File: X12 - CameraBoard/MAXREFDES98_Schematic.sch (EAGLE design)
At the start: 24 parts, among them U1 MB110S-TP, U2 MB110S-TP, U3 MAX5969AETB+, U4 MAX17503ATP+

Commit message: Added Net Labels & Mounting Holes
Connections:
- net N$1 renamed SV2_1
- net N$10 renamed PG_EN/UVLO
- net N$12 renamed RESET
- net N$13 renamed SS
- net N$14 renamed CF
- net N$16 renamed RT
- net N$17 renamed BST
- net N$18 renamed LX
- net N$19 renamed FB
- net N$2 renamed SV2_2
- net N$21 renamed SV1_1/2
- net N$25 renamed EPAD
- net N$3 renamed SV2_3
- net N$4 renamed SV2_4
- net N$5 renamed VDD
- net N$6 renamed VSS_EP
- net N$7 renamed DET
- net N$8 renamed CLS
- net N$9 renamed VIN

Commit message: rewiring
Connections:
- net N$11 renamed VCC
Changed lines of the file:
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@@
 </segment>
 </net>
-<net name="N$11" class="0">
+<net name="VCC" class="0">
 <segment>
 <pinref part="U4" gate="A" pin="VCC"/>

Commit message: Reconfigured Board Layout
Reconfigured Board Layout
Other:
- note added: "IC PoE CNTRL 1 Channel"
- note added: "IC REG BUCK"
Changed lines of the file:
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@@
 <sheet>
 <plain>
+<text x="137.16" y="7.62" size="1.778" layer="91">IC PoE CNTRL 1 Channel</text>
+<text x="-5.08" y="7.62" size="1.778" layer="91">IC REG BUCK</text>
 </plain>
 <instances>

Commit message: Update MAXREFDES98_Schematic.sch
Added frame and better labels
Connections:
- net SV1_1/2 renamed 5V_OUT
- net SV2_1 renamed RECT_A_INPUT_1
- net SV2_2 renamed RECT_A_INPUT_2
- net SV2_3 renamed RECT_B_INPUT_1
- net SV2_4 renamed RECT_B_INPUT_2
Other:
- note added: "Rectifiers"
- moved on the sheet: SV1
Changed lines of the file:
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@@
 <part name="GND13" library="supply1" library_urn="urn:adsk.eagle:library:371" deviceset="GND" device=""/>
 <part name="L1" library="SD53-3R3-R" deviceset="SD53-3R3-R" device=""/>
+<part name="FRAME1" library="frames" library_urn="urn:adsk.eagle:library:229" deviceset="FRAME_B_L" device=""/>
 </parts>
 <sheets>
 <sheet>
 <plain>
-<text x="137.16" y="7.62" size="1.778" layer="91">IC PoE CNTRL 1 Channel</text>
-<text x="-5.08" y="7.62" size="1.778" layer="91">IC REG BUCK</text>
+<text x="-7.62" y="10.16" size="1.778" layer="91">IC PoE CNTRL 1 Channel</text>
+<text x="142.24" y="7.62" size="1.778" layer="91">IC REG BUCK</text>
+<text x="-109.22" y="-7.62" size="1.778" layer="91">Rectifiers</text>
 </plain>
 <instances>
@@
 <attribute name="VALUE" x="-88.9" y="-5.08" size="1.27" layer="96" rot="R90"/>
 </instance>
-<instance part="SV1" gate="1" x="172.72" y="-86.36" smashed="yes" rot="MR90">
-<attribute name="VALUE" x="160.02" y="-87.63" size="1.778" layer="96" rot="MR90"/>
-<attribute name="NAME" x="181.102" y="-87.63" size="1.778" layer="95" rot="MR90"/>
+<instance part="SV1" gate="1" x="182.88" y="-73.66" smashed="yes" rot="MR90">
+<attribute name="VALUE" x="170.18" y="-74.93" size="1.778" layer="96" rot="MR90"/>
+<attribute name="NAME" x="191.262" y="-74.93" size="1.778" layer="95" rot="MR90"/>
 </instance>
 <instance part="SV2" gate="1" x="-106.68" y="-40.64" smashed="yes" rot="MR90">
@@
 <attribute name="VALUE" x="256.54" y="-48.26" size="1.778" layer="96" rot="MR0"/>
 </instance>
-<instance part="GND9" gate="1" x="170.18" y="-71.12" smashed="yes" rot="MR0">
-<attribute name="VALUE" x="172.72" y="-73.66" size="1.778" layer="96" rot="MR0"/>
+<instance part="GND9" gate="1" x="180.34" y="-58.42" smashed="yes" rot="MR0">
+<attribute name="VALUE" x="182.88" y="-60.96" size="1.778" layer="96" rot="MR0"/>
 </instance>
 <instance part="GND10" gate="1" x="226.06" y="-15.24" smashed="yes" rot="MR0">
@@
 <attribute name="NAME" x="55.88" y="24.13" size="1.778" layer="95" font="vector" rot="R90"/>
 <attribute name="VALUE" x="60.96" y="24.13" size="1.778" layer="96" font="vector" rot="R90" align="top-left"/>
+</instance>
+<instance part="FRAME1" gate="G$1" x="-139.7" y="-144.78" smashed="yes"/>
+<instance part="FRAME1" gate="G$2" x="185.42" y="-144.78" smashed="yes">
+<attribute name="LAST_DATE_TIME" x="198.12" y="-143.51" size="2.54" layer="94"/>
+<attribute name="SHEET" x="271.78" y="-143.51" size="2.54" layer="94"/>
+<attribute name="DRAWING_NAME" x="203.2" y="-125.73" size="2.54" layer="94"/>
 </instance>
 </instances>
@@
 </busses>
 <nets>
-<net name="SV2_1" class="0">
+<net name="RECT_A_INPUT_1" class="0">
 <segment>
 <pinref part="U1" gate="G$1" pin="~1"/>
@@
 </segment>
 </net>
-<net name="SV2_2" class="0">
+<net name="RECT_A_INPUT_2" class="0">
 <segment>
 <pinref part="U1" gate="G$1" pin="~2"/>
@@
 </segment>
 </net>
-<net name="SV2_3" class="0">
+<net name="RECT_B_INPUT_1" class="0">
 <segment>
 <pinref part="U2" gate="G$1" pin="~1"/>
@@
 </segment>
 </net>
-<net name="SV2_4" class="0">
+<net name="RECT_B_INPUT_2" class="0">
 <segment>
 <pinref part="U2" gate="G$1" pin="~2"/>
@@
 <junction x="-25.4" y="22.86"/>
 <pinref part="L1" gate="G$1" pin="1"/>
+<label x="10.16" y="22.86" size="1.778" layer="95"/>
 </segment>
 </net>
@@
 <wire x1="-45.72" y1="-12.7" x2="-45.72" y2="-27.94" width="0.1524" layer="91"/>
 <pinref part="R1" gate="G$1" pin="1"/>
-<wire x1="-101.6" y1="-25.4" x2="-101.6" y2="-33.02" width="0.1524" layer="91"/>
-<wire x1="38.1" y1="-25.4" x2="-101.6" y2="-25.4" width="0.1524" layer="91"/>
 <wire x1="-45.72" y1="-27.94" x2="38.1" y2="-27.94" width="0.1524" layer="91"/>
 <wire x1="38.1" y1="-27.94" x2="38.1" y2="-25.4" width="0.1524" layer="91"/>
-<junction x="38.1" y="-25.4"/>
 <pinref part="U3" gate="G$1" pin="VSS"/>
 <wire x1="-25.4" y1="-2.54" x2="-25.4" y2="-12.7" width="0.1524" layer="91"/>
@@
 <wire x1="-25.4" y1="-33.02" x2="-25.4" y2="-12.7" width="0.1524" layer="91"/>
 <junction x="-25.4" y="-12.7"/>
+<label x="7.62" y="-25.4" size="1.778" layer="95" rot="R180"/>
+<label x="-2.54" y="-33.02" size="1.778" layer="95"/>
+</segment>
+<segment>
 <pinref part="SV2" gate="1" pin="6"/>
+<wire x1="-101.6" y1="-25.4" x2="-101.6" y2="-33.02" width="0.1524" layer="91"/>
+<label x="-101.6" y="-25.4" size="1.778" layer="95" rot="R270"/>
 </segment>
 </net>
@@
 <wire x1="-104.14" y1="-20.32" x2="-104.14" y2="-33.02" width="0.1524" layer="91"/>
 <pinref part="SV2" gate="1" pin="5"/>
+<label x="2.54" y="-12.7" size="1.778" layer="95" rot="R180"/>
 </segment>
 </net>
@@
 <segment>
 <pinref part="U3" gate="G$1" pin="PG"/>
-<wire x1="30.48" y1="0" x2="58.42" y2="0" width="0.1524" layer="91"/>
+<wire x1="30.48" y1="0" x2="63.5" y2="0" width="0.1524" layer="91"/>
 <pinref part="R3" gate="G$1" pin="1"/>
-<wire x1="58.42" y1="0" x2="63.5" y2="0" width="0.1524" layer="91"/>
 <wire x1="63.5" y1="0" x2="63.5" y2="12.7" width="0.1524" layer="91"/>
 <pinref part="U4" gate="A" pin="EN/UVLO"/>
 <wire x1="63.5" y1="0" x2="119.38" y2="0" width="0.1524" layer="91"/>
 <junction x="63.5" y="0"/>
+<label x="45.72" y="0" size="1.778" layer="95"/>
 </segment>
 </net>
@@
 <pinref part="L1" gate="G$1" pin="2"/>
 <junction x="63.5" y="22.86"/>
+<label x="88.9" y="22.86" size="1.778" layer="95"/>
 </segment>
 </net>
@@
 <wire x1="180.34" y1="-15.24" x2="198.12" y2="-15.24" width="0.1524" layer="91"/>
 <pinref part="C8" gate="G$1" pin="1"/>
-</segment>
-</net>
-<net name="RESET" class="0">
-<segment>
-<pinref part="U4" gate="A" pin="!RESET"/>
-<wire x1="119.38" y1="-2.54" x2="96.52" y2="-2.54" width="0.1524" layer="91"/>
-<wire x1="96.52" y1="-2.54" x2="96.52" y2="-35.56" width="0.1524" layer="91"/>
-<wire x1="96.52" y1="-35.56" x2="177.8" y2="-35.56" width="0.1524" layer="91"/>
-<pinref part="SV1" gate="1" pin="6"/>
-<wire x1="177.8" y1="-35.56" x2="177.8" y2="-78.74" width="0.1524" layer="91"/>
-<label x="180.34" y="-66.04" size="1.778" layer="95" rot="R90"/>
 </segment>
 </net>
@@
 </segment>
 </net>
-<net name="SV1_1/2" class="0">
+<net name="5V_OUT" class="0">
 <segment>
 <pinref part="C4" gate="G$1" pin="1"/>
@@
 <wire x1="254" y1="0" x2="254" y2="-7.62" width="0.1524" layer="91"/>
 <junction x="238.76" y="0"/>
-<wire x1="266.7" y1="0" x2="266.7" y2="-58.42" width="0.1524" layer="91"/>
-<wire x1="266.7" y1="-58.42" x2="165.1" y2="-58.42" width="0.1524" layer="91"/>
 <wire x1="254" y1="0" x2="266.7" y2="0" width="0.1524" layer="91"/>
 <junction x="254" y="0"/>
+<label x="266.7" y="2.54" size="1.778" layer="95" rot="R180"/>
+</segment>
+<segment>
+<pinref part="SV1" gate="1" pin="2"/>
+<wire x1="177.8" y1="-60.96" x2="177.8" y2="-66.04" width="0.1524" layer="91"/>
+<wire x1="175.26" y1="-60.96" x2="177.8" y2="-60.96" width="0.1524" layer="91"/>
 <pinref part="SV1" gate="1" pin="1"/>
-<wire x1="165.1" y1="-78.74" x2="165.1" y2="-73.66" width="0.1524" layer="91"/>
-<wire x1="165.1" y1="-73.66" x2="165.1" y2="-58.42" width="0.1524" layer="91"/>
-<wire x1="165.1" y1="-73.66" x2="167.64" y2="-73.66" width="0.1524" layer="91"/>
-<junction x="165.1" y="-73.66"/>
-<pinref part="SV1" gate="1" pin="2"/>
-<wire x1="167.64" y1="-73.66" x2="167.64" y2="-78.74" width="0.1524" layer="91"/>
-<label x="162.56" y="-58.42" size="1.778" layer="95" rot="R270"/>
+<wire x1="175.26" y1="-66.04" x2="175.26" y2="-60.96" width="0.1524" layer="91"/>
+<wire x1="175.26" y1="-60.96" x2="175.26" y2="-50.8" width="0.1524" layer="91"/>
+<junction x="175.26" y="-60.96"/>
+<label x="175.26" y="-58.42" size="1.778" layer="95" rot="R90"/>
 </segment>
 </net>
@@
 <segment>
 <pinref part="SV1" gate="1" pin="3"/>
-<wire x1="170.18" y1="-78.74" x2="170.18" y2="-73.66" width="0.1524" layer="91"/>
-<wire x1="170.18" y1="-73.66" x2="172.72" y2="-73.66" width="0.1524" layer="91"/>
+<wire x1="180.34" y1="-66.04" x2="180.34" y2="-60.96" width="0.1524" layer="91"/>
+<wire x1="180.34" y1="-60.96" x2="182.88" y2="-60.96" width="0.1524" layer="91"/>
 <pinref part="SV1" gate="1" pin="4"/>
-<wire x1="172.72" y1="-73.66" x2="172.72" y2="-78.74" width="0.1524" layer="91"/>
-<wire x1="172.72" y1="-73.66" x2="172.72" y2="-63.5" width="0.1524" layer="91"/>
-<junction x="172.72" y="-73.66"/>
-<wire x1="172.72" y1="-63.5" x2="170.18" y2="-63.5" width="0.1524" layer="91"/>
-<wire x1="170.18" y1="-63.5" x2="170.18" y2="-66.04" width="0.1524" layer="91"/>
+<wire x1="182.88" y1="-60.96" x2="182.88" y2="-66.04" width="0.1524" layer="91"/>
+<wire x1="182.88" y1="-60.96" x2="182.88" y2="-50.8" width="0.1524" layer="91"/>
+<junction x="182.88" y="-60.96"/>
+<wire x1="182.88" y1="-50.8" x2="180.34" y2="-50.8" width="0.1524" layer="91"/>
 <pinref part="GND9" gate="1" pin="GND"/>
-<wire x1="170.18" y1="-66.04" x2="170.18" y2="-68.58" width="0.1524" layer="91"/>
+<wire x1="180.34" y1="-50.8" x2="180.34" y2="-55.88" width="0.1524" layer="91"/>
 </segment>
 <segment>
@@
 </segment>
 </net>
+<net name="RESET" class="0">
+<segment>
+<pinref part="SV1" gate="1" pin="6"/>
+<wire x1="187.96" y1="-66.04" x2="187.96" y2="-60.96" width="0.1524" layer="91"/>
+<label x="190.5" y="-66.04" size="1.778" layer="95" rot="R90"/>
+</segment>
+<segment>
+<pinref part="U4" gate="A" pin="!RESET"/>
+<wire x1="119.38" y1="-2.54" x2="96.52" y2="-2.54" width="0.1524" layer="91"/>
+<label x="96.52" y="-2.54" size="1.778" layer="95" rot="R180"/>
+</segment>
+</net>

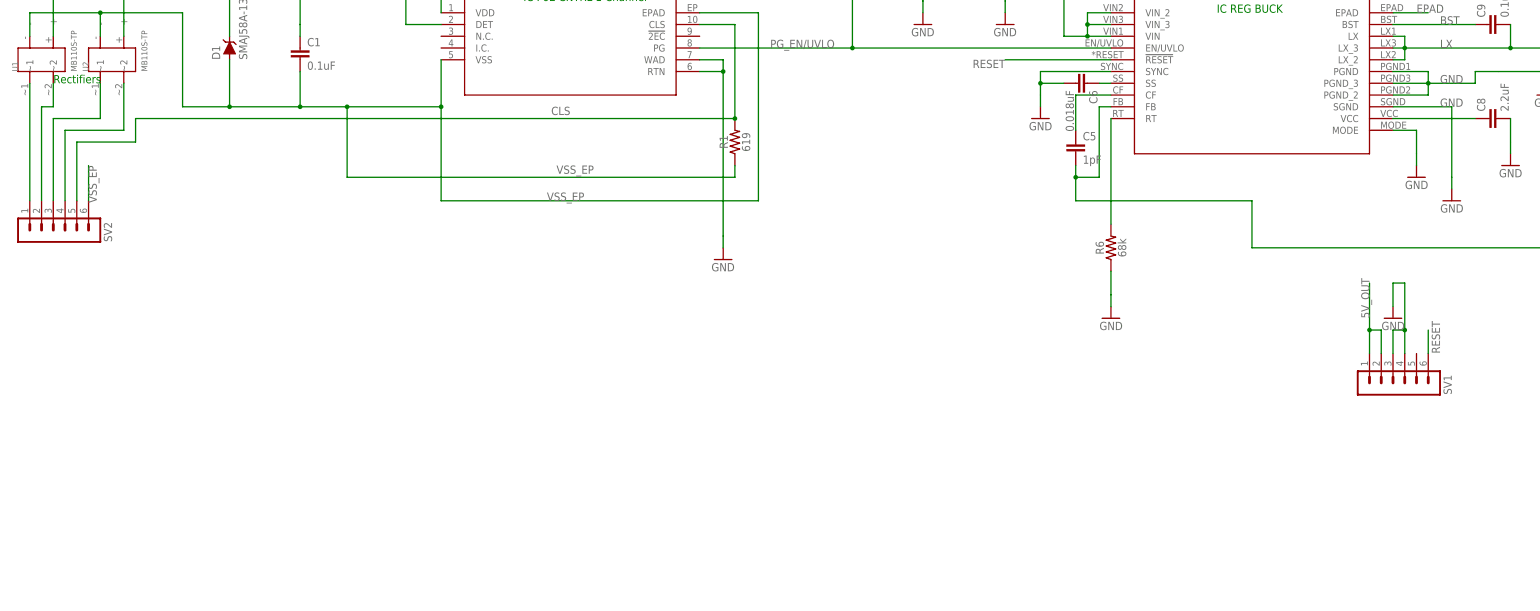
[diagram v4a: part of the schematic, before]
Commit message: Added New Connector and PI
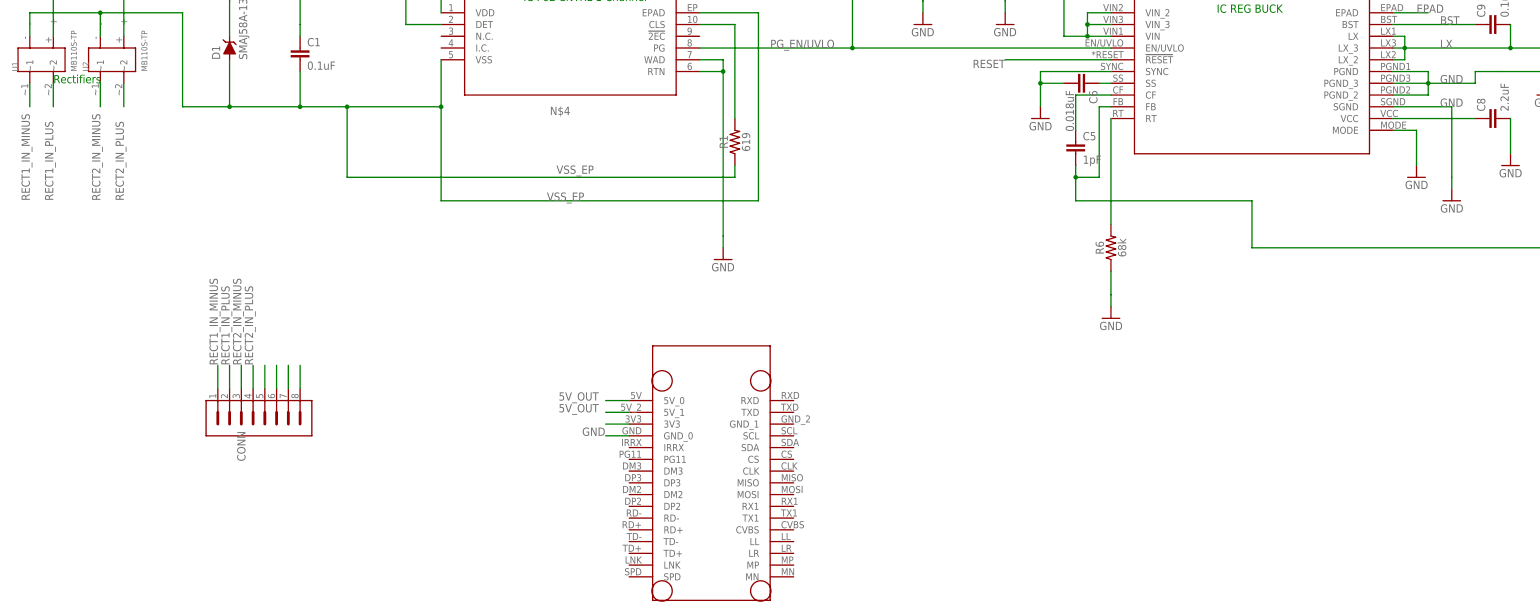
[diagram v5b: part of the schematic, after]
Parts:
- removed SV1, SV2: (no value), con-lstb:MA06-1
- added CONN: TERM_BLOCK_PLUG_8POS_STR_2.5MM, Camera_Board_Parts_09_30_2020:TERM_BLOCK_PLUG_8POS_STR_2.5MM
- added U$2: NANO_PI, Camera_Board_Parts_09_30_2020:NANO_PI
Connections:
- removed net CLS: R1.2, SV2.5, U3.CLS
- removed net RECT_A_INPUT_1: SV2.1, U1.~1
- removed net RECT_A_INPUT_2: SV2.2, U1.~2
- removed net RECT_B_INPUT_1: SV2.3, U2.~1
- removed net RECT_B_INPUT_2: SV2.4, U2.~2
- new net 5V_OUT5: CONN.5
- new net N$4: R1.2, U3.CLS
- new net N$8: U$2.3V3
- new net RECT1_IN_MINUS: CONN.1, U1.~1
- new net RECT1_IN_PLUS: CONN.2, U1.~2
- new net RECT2_IN_MINUS: CONN.3, U2.~1
- new net RECT2_IN_PLUS: CONN.4, U2.~2
- net 5V_OUT: now also CONN.6, U$2.5V_0, U$2.5V_1; no longer SV1.1, SV1.2
- net GND: now also CONN.7, CONN.8, U$2.GND_0; no longer SV1.3, SV1.4
- net RESET: no longer SV1.6
- net VSS_EP: no longer SV2.6
